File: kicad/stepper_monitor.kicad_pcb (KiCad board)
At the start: 2 copper layers, 38.5 x 43 mm, 52 parts, among them J1 Conn_01x04_Male, J2 Conn_01x04_Male, J3 Conn_01x02_Male, J4 USB_C_Receptacle_USB2.0, J5 JTAG, Q1 UMH3N, Q2 PJA3439, SW1 SW_Push, U1 CP2102N-A01-GQFN28, U2 AMS1117-3.3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

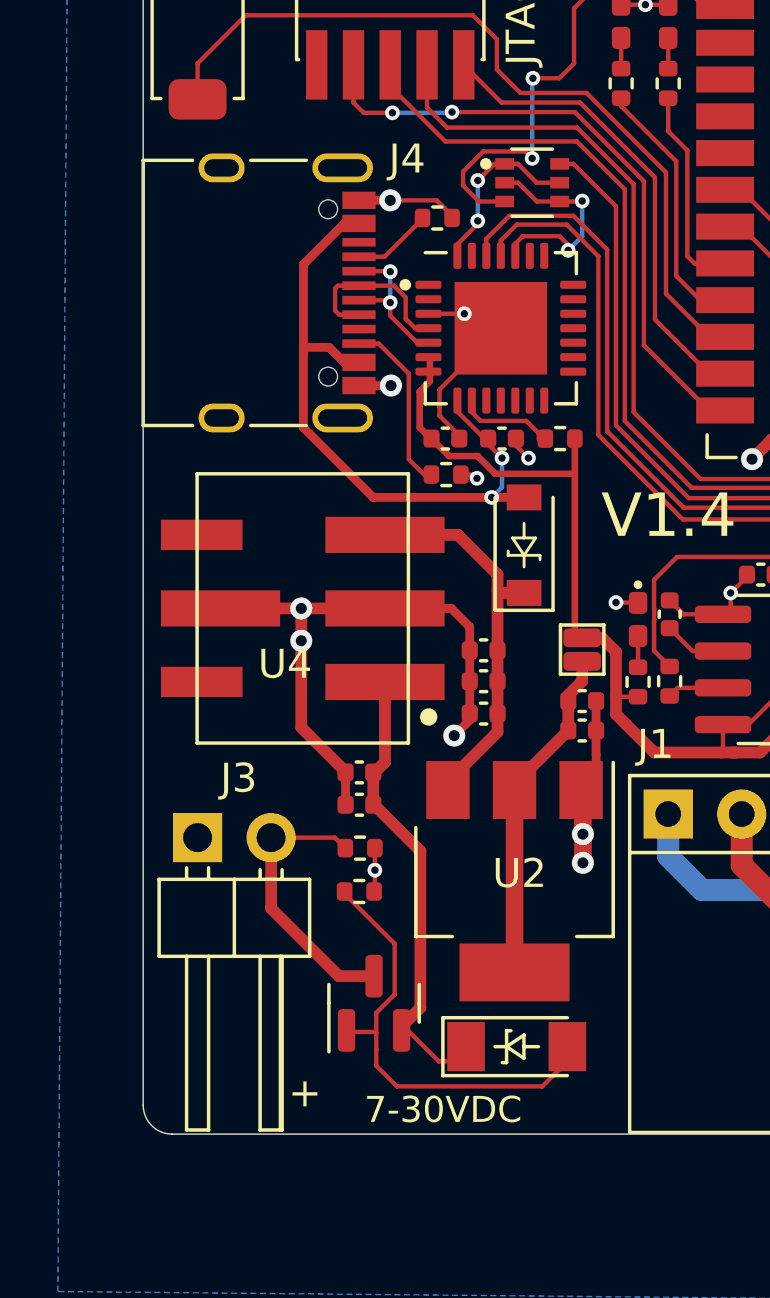
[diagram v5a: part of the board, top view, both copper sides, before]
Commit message: Connected USB shield to ground.
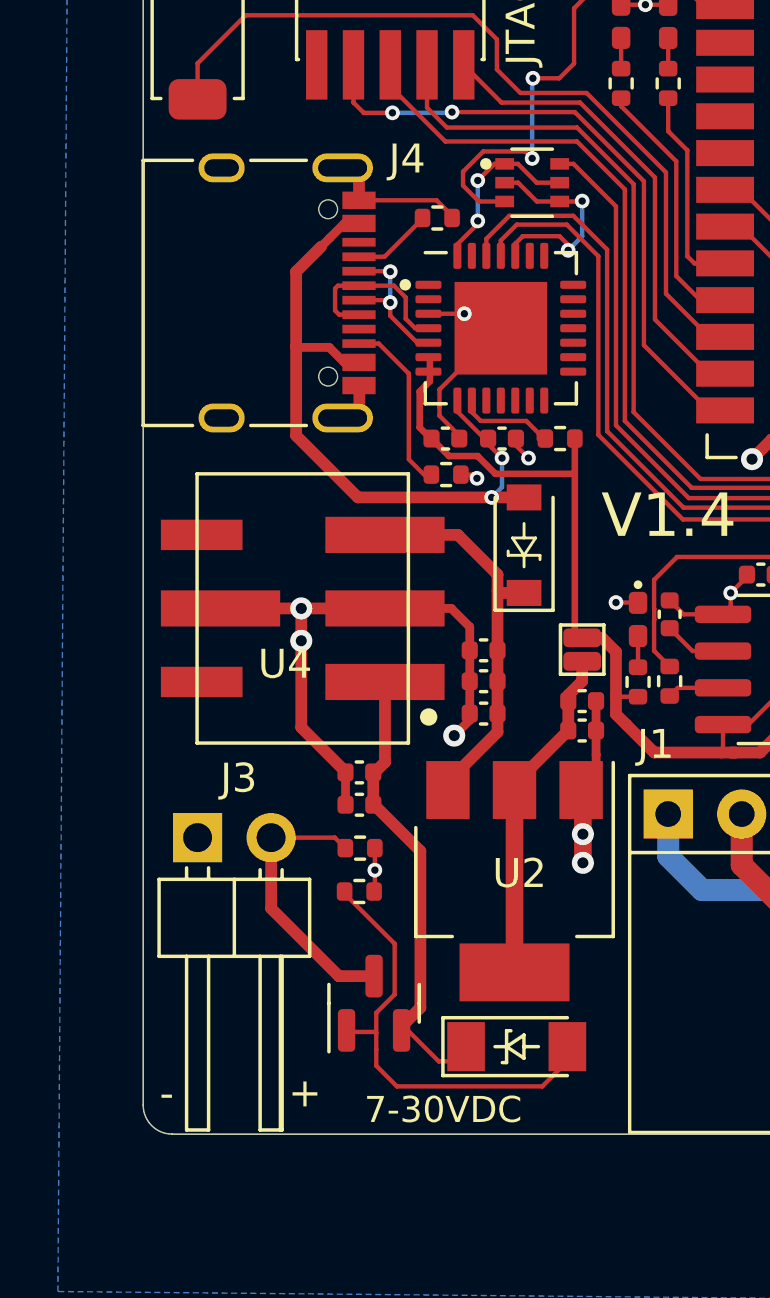
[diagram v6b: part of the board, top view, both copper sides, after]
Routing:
- net VBUS: track 23.2 -> 23.9 mm
- net GNDD: track 75.6 -> 75.5 mm, vias 22 -> 20
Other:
- board text added: "-"

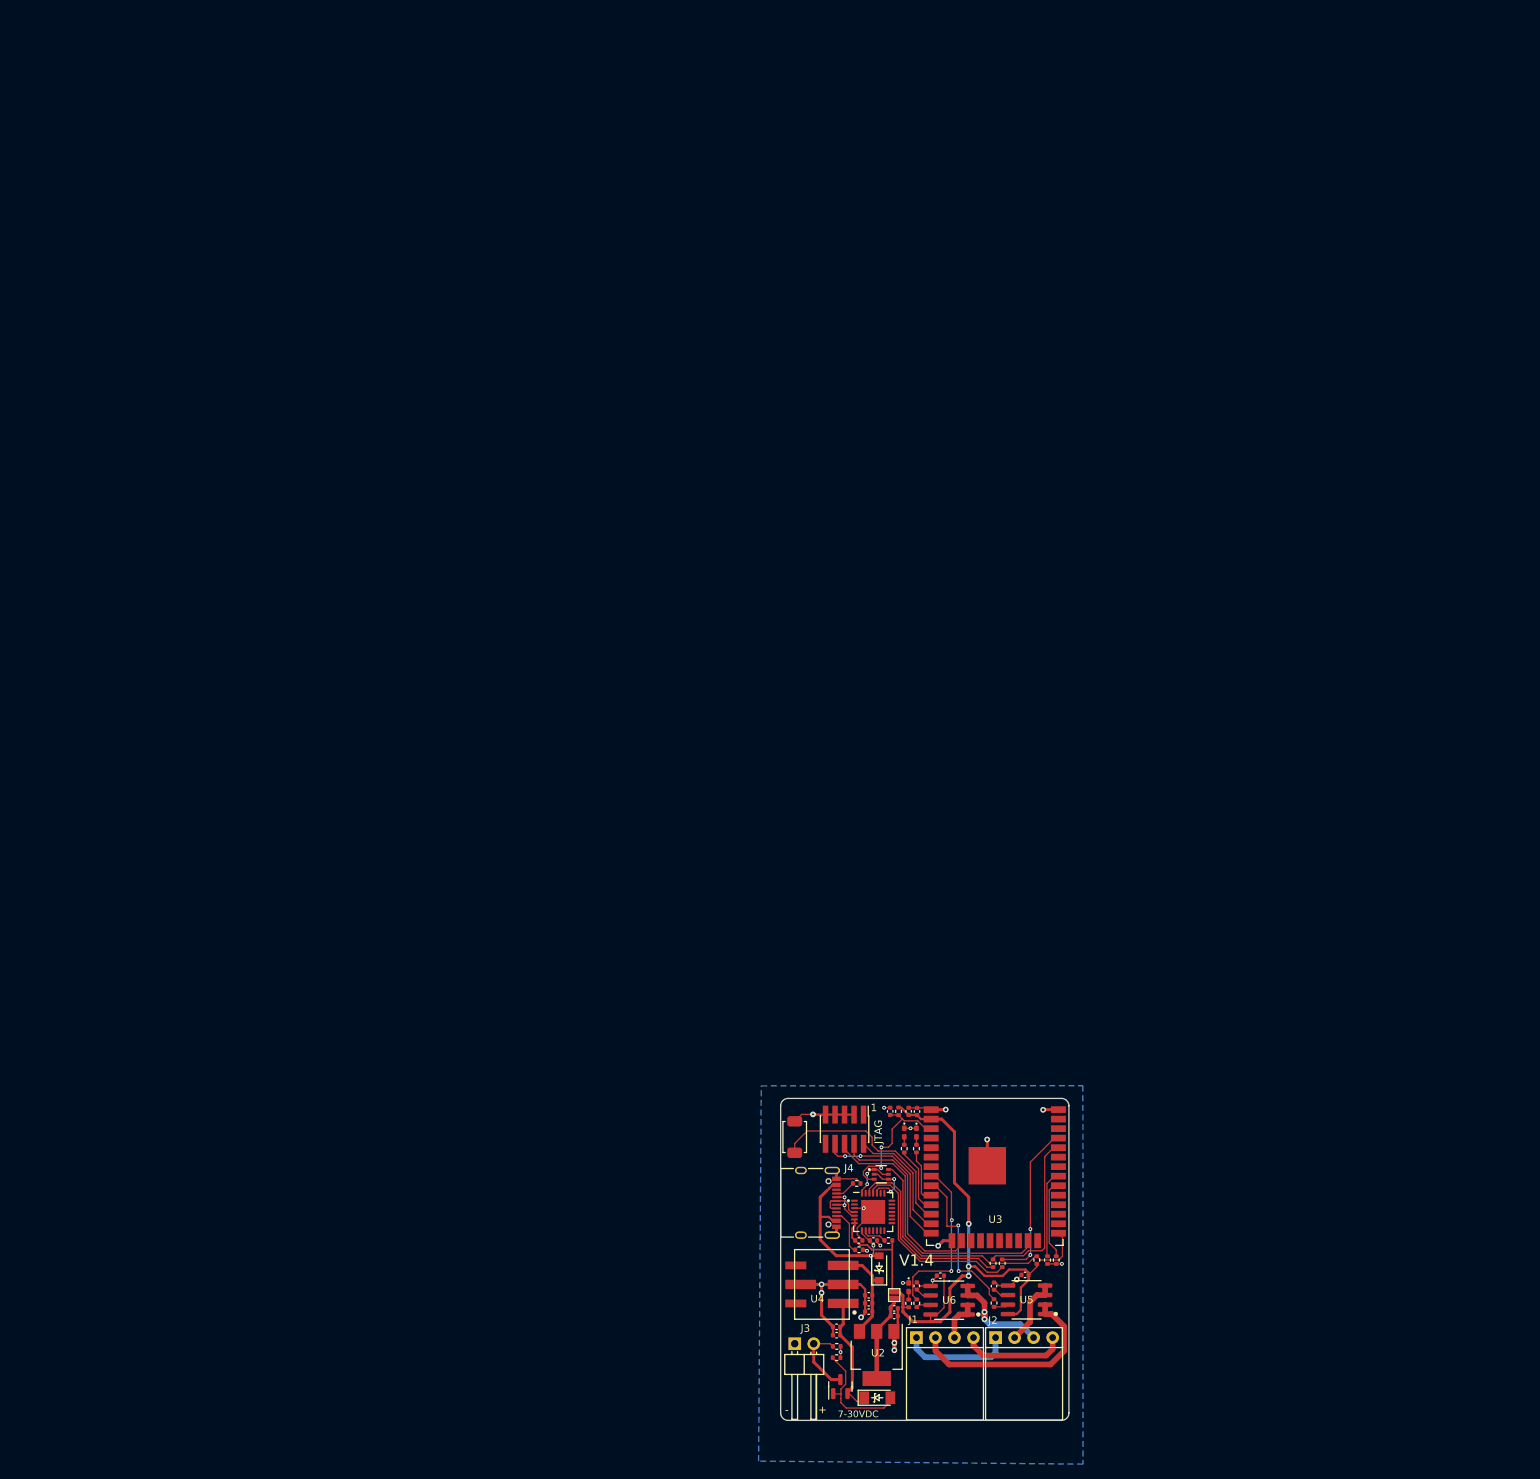
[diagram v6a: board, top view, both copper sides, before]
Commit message: Cleaned up the PCB layout.
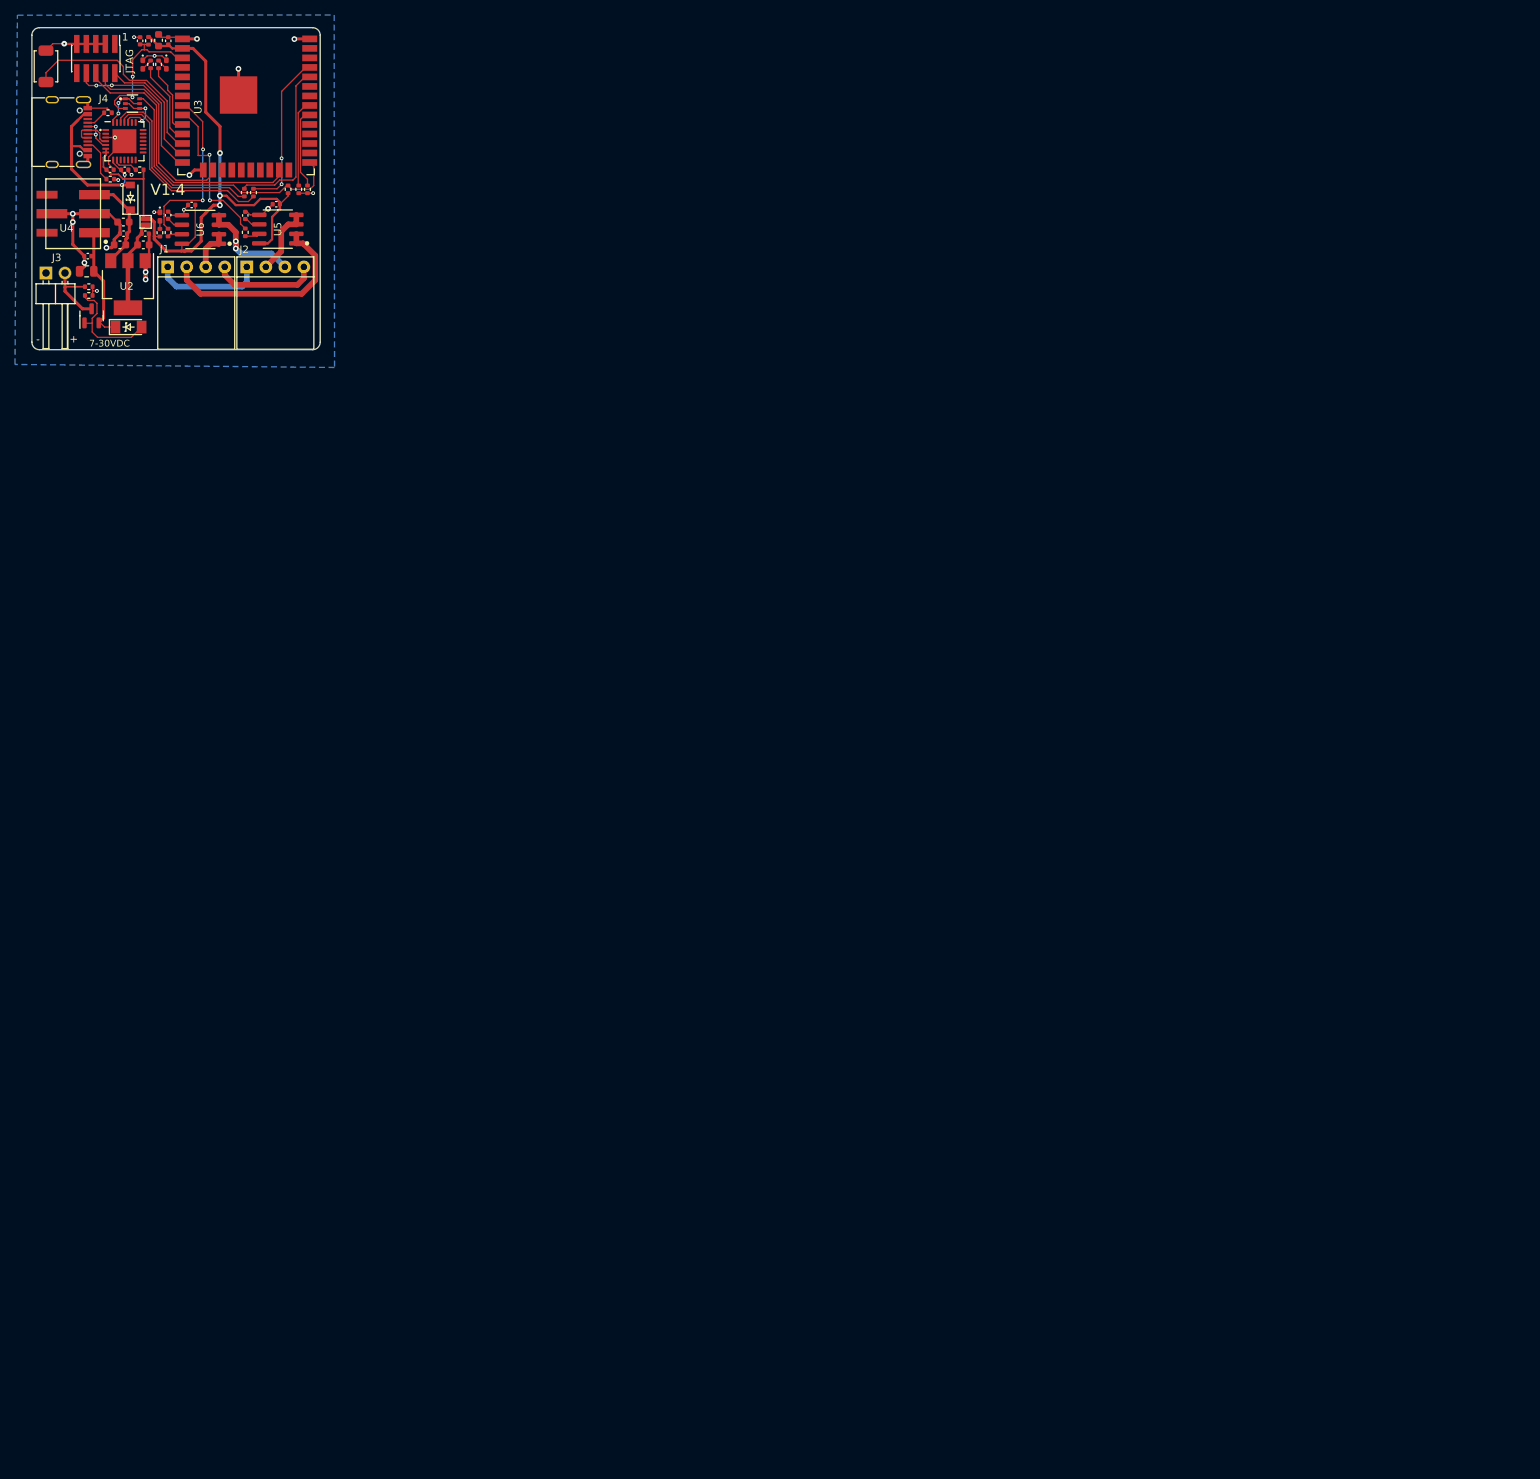
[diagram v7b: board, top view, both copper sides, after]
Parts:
- C10, C16, C3, C9: footprint Capacitor_SMD:C_0402_1005Metric -> Capacitor_SMD:C_0603_1608Metric
- C2: footprint Capacitor_SMD:C_0402_1005Metric -> Capacitor_SMD:C_0805_2012Metric
- Q2: footprint Package_TO_SOT_SMD:SOT-23 -> stepper_monitor:SOT-23
- moved R5 176.7 mm to (16.9, -38.1)
- moved R4 176.4 mm to (15.8, -38.1)
- moved D1 175.2 mm to (14.8, -38.1)
- moved C4 175.0 mm to (15.1, -15.5)
- moved JP1 174.8 mm to (15.2, -17.1)
- moved C3 174.7 mm to (14.9, -14.0)
- moved U4 174.7 mm to (5.23, -18.2)
- moved C16 174.6 mm to (16.9, -41.3)
- moved R7 174.6 mm to (15.6, -41.3)
- moved C7 174.6 mm to (14.5, -41.2)
- moved C10 174.5 mm to (12.2, -17.0)
- moved C11 174.5 mm to (32.6, -19.4)
- moved C12 174.5 mm to (28.5, -17.9)
- moved C13 174.5 mm to (21.3, -19.3)
- moved C14 174.5 mm to (18.2, -18.0)
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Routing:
- net GNDD: track 75.5 -> 80.5 mm, vias 20 -> 21
- net LED2: track 6.86 -> 9.46 mm
- net LED1: track 8.96 -> 11.0 mm
- net Net-(D5-Pad2): track 15.9 -> 14.7 mm
- net Net-(C2-Pad2): track 16.3 -> 15.3 mm
- net EN: track 19.4 -> 20.2 mm

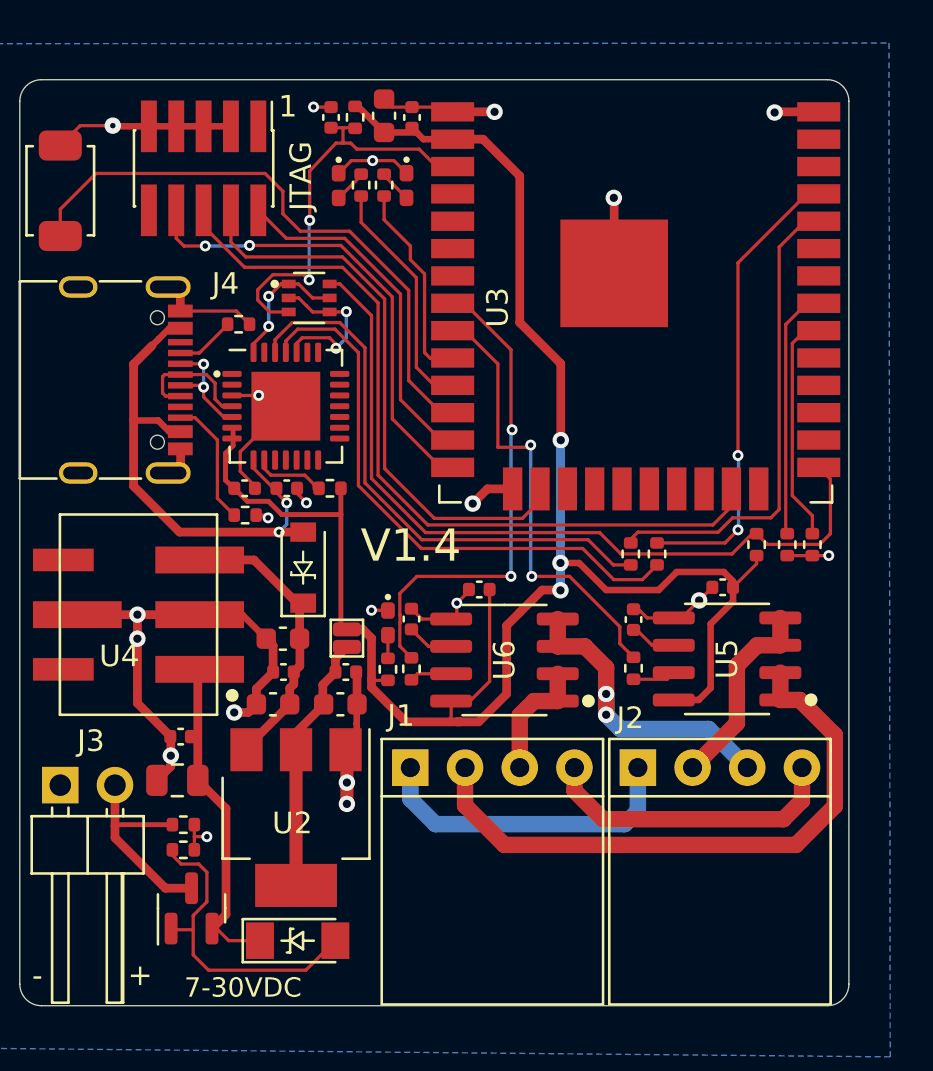
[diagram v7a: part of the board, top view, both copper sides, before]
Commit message: Minor PCB layout tweaks.
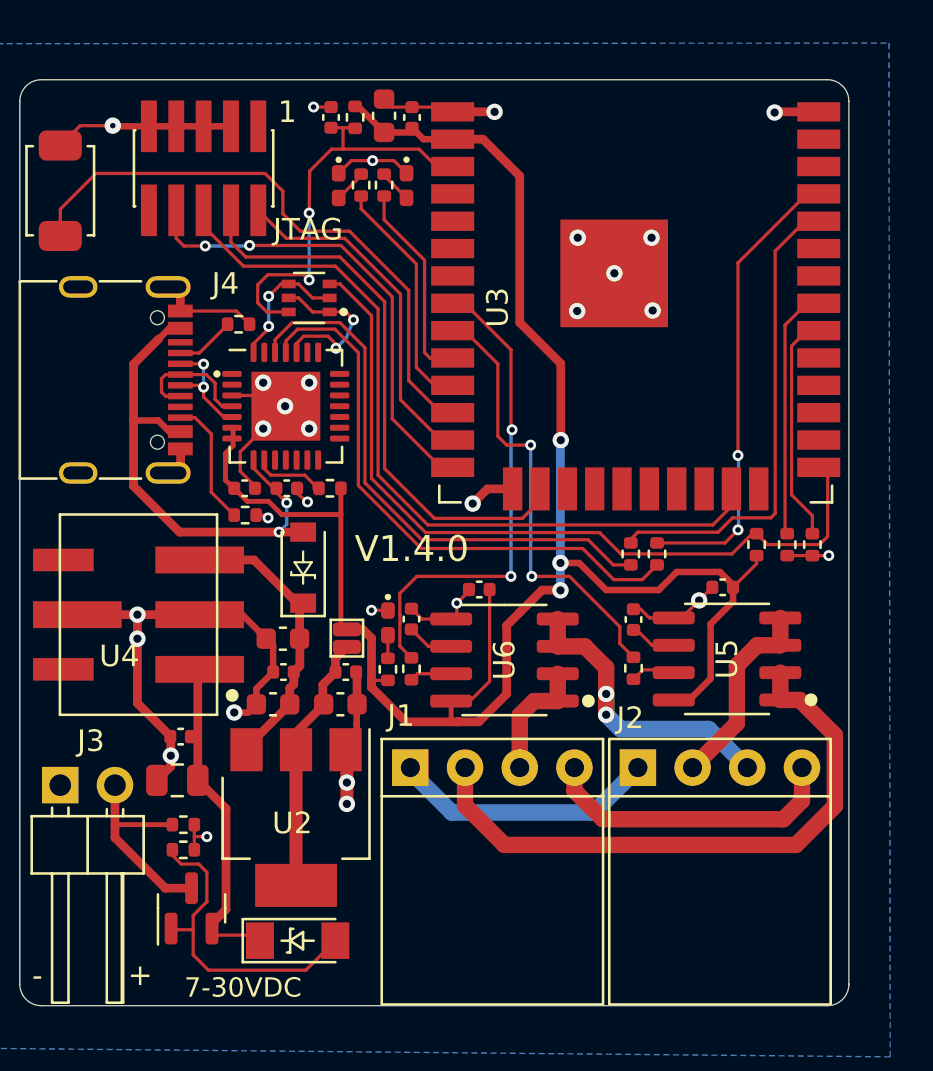
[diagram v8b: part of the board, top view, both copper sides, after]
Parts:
- turned Q1 to 180 degrees
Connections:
- Q1 pad 1: DTR -> RTS
- Q1 pad 2: RTS -> DTR
- Q1 pad 3: EN -> IO0
- Q1 pad 4: RTS -> DTR
- Q1 pad 5: DTR -> RTS
- Q1 pad 6: IO0 -> EN
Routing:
- net GNDD: track 80.5 -> 77.0 mm, vias 21 -> 29
- net Net-(J1-Pad1): track 14.8 -> 12.4 mm
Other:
- board text added: "STEPPER MOTOR ANALYZER ESP32, OSH, github/zapta"
- board text added: "V1.4.0"
- board text removed: "STEPPER MOTOR ANALYZER V1.4 ESP32 OSH, github/zapta"
- board text removed: "V1.4"
